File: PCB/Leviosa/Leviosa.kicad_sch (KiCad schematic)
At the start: 24 parts, among them Q3 TIP122, Q4 TIP122, U1 LM324, U5 L7805, U6 SS495A

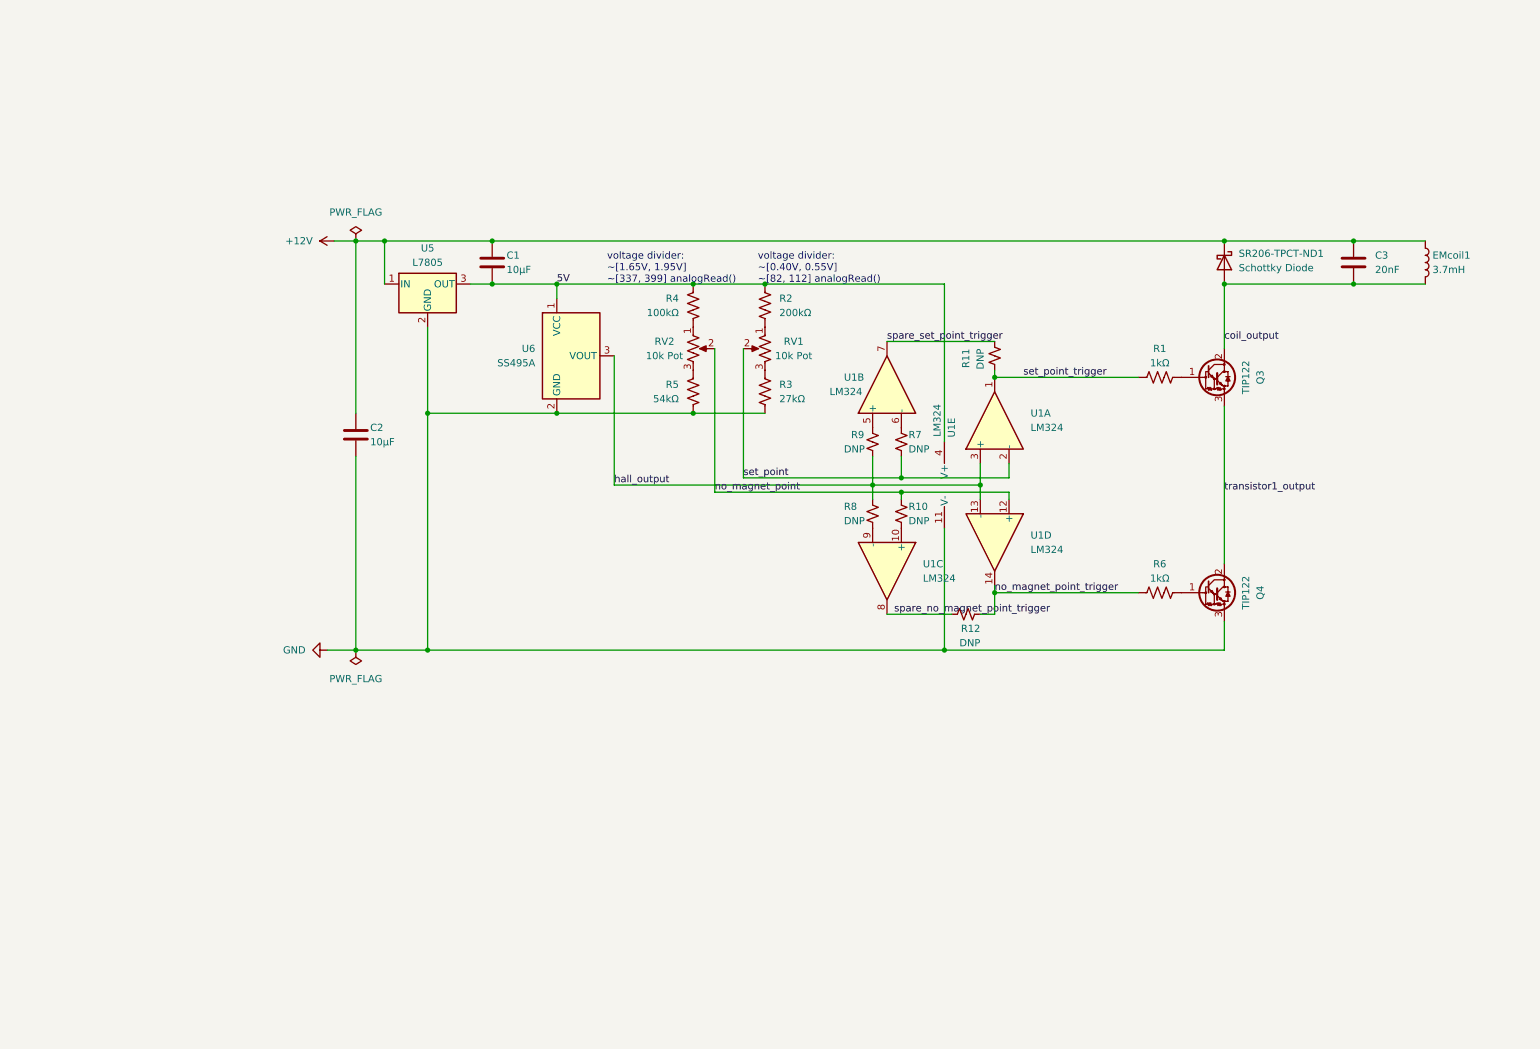
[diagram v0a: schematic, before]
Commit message: added attiny and load switch. Still need power input.
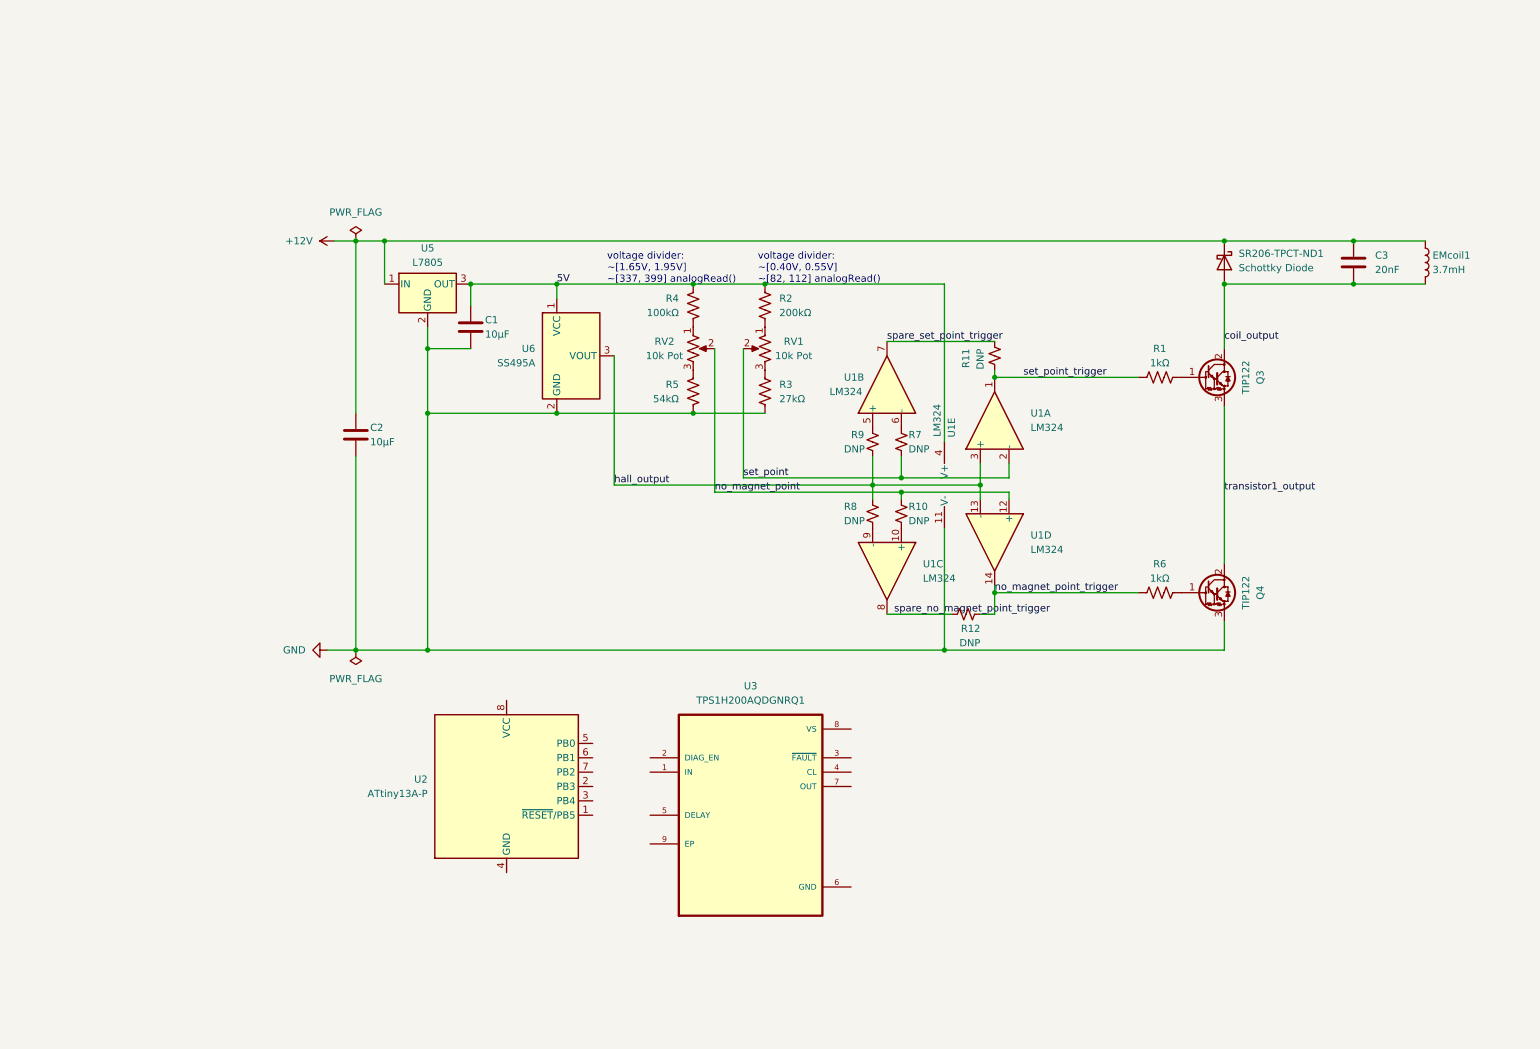
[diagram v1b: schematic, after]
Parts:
- added U2: ATtiny13A-P, Package_DIP:DIP-8_W7.62mm, symbol MCU_Microchip_ATtiny:ATtiny13A-P
- added U3: TPS1H200AQDGNRQ1, TPS1H200AQDGNRQ1:SOP65P490X110-9N, symbol TPS1H200AQDGNRQ1:TPS1H200AQDGNRQ1
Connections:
- net +12V: no longer C1.1
- net 5V: now also C1.1; no longer C1.2
- net GND: now also C1.2
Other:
- moved on the sheet: C1
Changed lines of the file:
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@@
   (junction (at 187.96 116.84) (diameter 0) (color 0 0 0 0)
   )
+  (junction (at 95.25 62.23) (diameter 0) (color 0 0 0 0)
+  )
   (junction (at 110.49 62.23) (diameter 0) (color 0 0 0 0)
   )
   (junction (at 228.6 62.23) (diameter 0) (color 0 0 0 0)
   )
-  (junction (at 99.06 62.23) (diameter 0) (color 0 0 0 0)
-  )
   (junction (at 87.63 127) (diameter 0) (color 0 0 0 0)
   )
@@
   (junction (at 171.45 99.06) (diameter 0) (color 0 0 0 0)
   )
-  (junction (at 99.06 54.61) (diameter 0) (color 0 0 0 0)
-  )
   (junction (at 110.49 85.09) (diameter 0) (color 0 0 0 0)
   )
+  (junction (at 87.63 73.66) (diameter 0) (color 0 0 0 0)
+  )
   (junction (at 74.93 127) (diameter 0) (color 0 0 0 0)
   )
@@
     (stroke (width 0) (type default))
   )
+  (wire (pts (xy 87.63 73.66) (xy 95.25 73.66))
+    (stroke (width 0) (type default))
+  )
   (wire (pts (xy 166.37 100.33) (xy 166.37 97.79))
     (stroke (width 0) (type default))
@@
     (stroke (width 0) (type default))
   )
-  (wire (pts (xy 80.01 54.61) (xy 99.06 54.61))
+  (wire (pts (xy 80.01 54.61) (xy 228.6 54.61))
     (stroke (width 0) (type default))
   )
@@
     (stroke (width 0) (type default))
   )
-  (wire (pts (xy 95.25 62.23) (xy 99.06 62.23))
+  (wire (pts (xy 95.25 62.23) (xy 110.49 62.23))
     (stroke (width 0) (type default))
   )
@@
     (stroke (width 0) (type default))
   )
+  (wire (pts (xy 87.63 73.66) (xy 87.63 85.09))
+    (stroke (width 0) (type default))
+  )
   (wire (pts (xy 87.63 85.09) (xy 110.49 85.09))
     (stroke (width 0) (type default))
@@
     (stroke (width 0) (type default))
   )
-  (wire (pts (xy 110.49 62.23) (xy 99.06 62.23))
+  (wire (pts (xy 95.25 62.23) (xy 95.25 66.04))
     (stroke (width 0) (type default))
   )
@@
     (stroke (width 0) (type default))
   )
-  (wire (pts (xy 99.06 54.61) (xy 228.6 54.61))
-    (stroke (width 0) (type default))
-  )
   (wire (pts (xy 74.93 92.71) (xy 74.93 127))
     (stroke (width 0) (type default))
@@
     (stroke (width 0) (type default))
   )
-  (wire (pts (xy 87.63 69.85) (xy 87.63 85.09))
+  (wire (pts (xy 87.63 69.85) (xy 87.63 73.66))
     (stroke (width 0) (type default))
   )
@@
     )
   )
-  (symbol (lib_id "Device:C") (at 99.06 58.42 0) (unit 1)
-    (in_bom yes) (on_board yes) (dnp no)
-    (property "Reference" "C1" (at 101.6 57.15 0)
-      (effects (font (size 1.27 1.27)) (justify left))
-    )
-    (property "Value" "10µF" (at 101.6 59.69 0)
-      (effects (font (size 1.27 1.27)) (justify left))
-    )
-    (property "Footprint" "Capacitor_THT:CP_Axial_L10.0mm_D6.0mm_P15.00mm_Horizontal" (at 100.0252 62.23 0)
-      (effects (font (size 1.27 1.27)) hide)
-    )
-    (property "Datasheet" "~" (at 99.06 58.42 0)
+  (symbol (lib_id "Device:C") (at 95.25 69.85 0) (unit 1)
+    (in_bom yes) (on_board yes) (dnp no)
+    (property "Reference" "C1" (at 97.79 68.58 0)
+      (effects (font (size 1.27 1.27)) (justify left))
+    )
+    (property "Value" "10µF" (at 97.79 71.12 0)
+      (effects (font (size 1.27 1.27)) (justify left))
+    )
+    (property "Footprint" "Capacitor_THT:CP_Axial_L10.0mm_D6.0mm_P15.00mm_Horizontal" (at 96.2152 73.66 0)
+      (effects (font (size 1.27 1.27)) hide)
+    )
+    (property "Datasheet" "~" (at 95.25 69.85 0)
       (effects (font (size 1.27 1.27)) hide)
     )
@@
     )
   )
+  (symbol (lib_id "MCU_Microchip_ATtiny:ATtiny13A-P") (at 101.6 151.13 0) (unit 1)
+    (in_bom yes) (on_board yes) (dnp no) (fields_autoplaced)
+    (property "Reference" "U2" (at 87.63 149.86 0)
+      (effects (font (size 1.27 1.27)) (justify right))
+    )
+    (property "Value" "ATtiny13A-P" (at 87.63 152.4 0)
+      (effects (font (size 1.27 1.27)) (justify right))
+    )
+    (property "Footprint" "Package_DIP:DIP-8_W7.62mm" (at 101.6 151.13 0)
+      (effects (font (size 1.27 1.27) italic) hide)
+    )
+    (property "Datasheet" "http://ww1.microchip.com/downloads/en/DeviceDoc/doc8126.pdf" (at 101.6 151.13 0)
+      (effects (font (size 1.27 1.27)) hide)
+    )
+    (pin "1")
+    (pin "2")
+    (pin "3")
+    (pin "4")
+    (pin "5")
+    (pin "6")
+    (pin "7")
+    (pin "8")
+    (instances
+      (project "Leviosa"
+        (path "/fe766911-203b-467c-b704-d4bd488f6c98"
+          (reference "U2") (unit 1)
+        )
+      )
+    )
+  )
   (symbol (lib_id "Device:C") (at 251.46 58.42 0) (unit 1)
     (in_bom yes) (on_board yes) (dnp no) (fields_autoplaced)
@@
         )
       )
+    )
+  )
+  (symbol (lib_id "TPS1H200AQDGNRQ1:TPS1H200AQDGNRQ1") (at 144.78 156.21 0) (unit 1)
+    (in_bom yes) (on_board yes) (dnp no) (fields_autoplaced)
+    (property "Reference" "U3" (at 144.78 133.35 0)
+      (effects (font (size 1.27 1.27)))
+    )
+    (property "Value" "TPS1H200AQDGNRQ1" (at 144.78 135.89 0)
+      (effects (font (size 1.27 1.27)))
+    )
+    (property "Footprint" "TPS1H200AQDGNRQ1:SOP65P490X110-9N" (at 144.78 156.21 0)
+      (effects (font (size 1.27 1.27)) (justify bottom) hide)
+    )
+    (property "Datasheet" "" (at 144.78 156.21 0)
+      (effects (font (size 1.27 1.27)) hide)
+    )
+    (property "SNAPEDA_LINK" "https://www.snapeda.com/parts/TPS1H200AQDGNRQ1/Texas+Instruments/view-part/?ref=snap" (at 144.78 156.21 0)
+      (effects (font (size 1.27 1.27)) (justify bottom) hide)
+    )
+    (property "CHECK_PRICES" "https://www.snapeda.com/parts/TPS1H200AQDGNRQ1/Texas+Instruments/view-part/?ref=eda" (at 144.78 156.21 0)
+      (effects (font (size 1.27 1.27)) (justify bottom) hide)
+    )
+    (property "PURCHASE-URL" "https://www.snapeda.com/api/url_track_click_mouser/?unipart_id=3210362&manufacturer=Texas Instruments&part_name=TPS1H200AQDGNRQ1&search_term=tps1h200aqdgnrq1" (at 144.78 156.21 0)
+      (effects (font (size 1.27 1.27)) (justify bottom) hide)
+    )
+    (property "PACKAGE" "HVSSOP-8 Texas Instruments" (at 144.78 156.21 0)
+      (effects (font (size 1.27 1.27)) (justify bottom) hide)
+    )
+    (property "PRICE" "None" (at 144.78 156.21 0)
+      (effects (font (size 1.27 1.27)) (justify bottom) hide)
+    )
+    (property "MF" "Texas Instruments" (at 144.78 156.21 0)
+      (effects (font (size 1.27 1.27)) (justify bottom) hide)
+    )
+    (property "MP" "TPS1H200AQDGNRQ1" (at 144.78 156.21 0)
+      (effects (font (size 1.27 1.27)) (justify bottom) hide)
+    )
+    (property "AVAILABILITY" "In Stock" (at 144.78 156.21 0)
+      (effects (font (size 1.27 1.27)) (justify bottom) hide)
+    )
+    (property "DESCRIPTION" "40-V, 200-mΩ, 1-ch automotive smart high-side switch with adjustable current limit" (at 144.78 156.21 0)
+      (effects (font (size 1.27 1.27)) (justify bottom) hide)
+    )
+    (pin "1")
+    (pin "2")
+    (pin "3")
+    (pin "4")
+    (pin "5")
+    (pin "6")
+    (pin "7")
+    (pin "8")
+    (pin "9")
+    (instances
+      (project "Leviosa"
+        (path "/fe766911-203b-467c-b704-d4bd488f6c98"
+          (reference "U3") (unit 1)
+        )
+      )

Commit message: added wiring for load switch in schematic
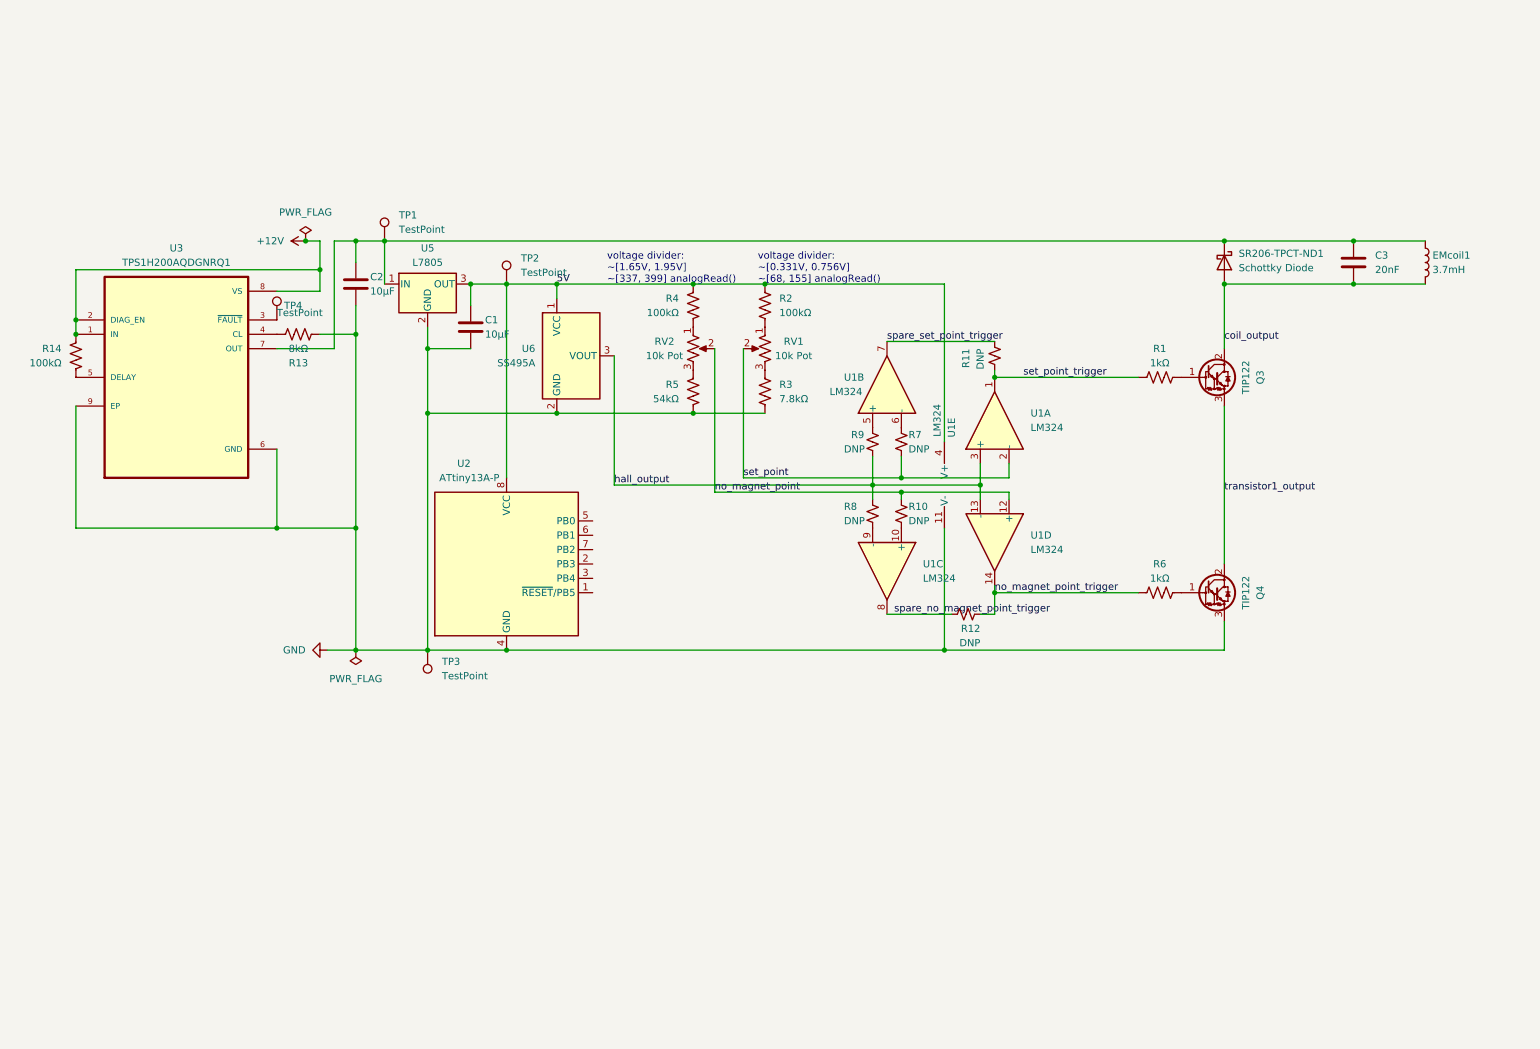
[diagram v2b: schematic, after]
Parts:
- added R13: 8kΩ, Resistor_THT:R_Axial_DIN0411_L9.9mm_D3.6mm_P12.70mm_Horizontal, symbol Device:R_US
- added R14: 100kΩ, Resistor_THT:R_Axial_DIN0411_L9.9mm_D3.6mm_P12.70mm_Horizontal, symbol Device:R_US
- added TP1, TP2, TP3, TP4: TestPoint, symbol Connector:TestPoint
- R2: value 200kΩ -> 100kΩ
- R3: value 27kΩ -> 7.8kΩ
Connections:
- net +12V: now also U3.1 (IN), U3.2 (DIAG_EN), U3.8 (VS), R14.2; no longer C2.1, C3.1, EMcoil1.1, SR206-TPCT-ND1.1 (K), U5.1 (IN)
- net 5V: now also U2.8 (VCC), TP2.1
- net GND: now also U2.4 (GND), U3.6 (GND), U3.9 (EP), R13.1, TP3.1
- net at U3.3 (~{FAULT}): now also TP4.1
- net at U3.4 (CL): now also R13.2
- net at U3.5 (DELAY): now also R14.1
- net at U3.7 (OUT): now also C2.1, C3.1, EMcoil1.1, SR206-TPCT-ND1.1 (K), U5.1 (IN), TP1.1
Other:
- note added: "voltage divider: ~[0.331V, 0.756V] ~[68, 155] analogRead()"
- note removed: "voltage divider: ~[0.40V, 0.55V] ~[82, 112] analogRead()"
- moved on the sheet: C2, U2, U3
